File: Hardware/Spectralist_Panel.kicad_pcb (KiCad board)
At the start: 2 copper layers, 60.8 x 128.5 mm, 24 parts

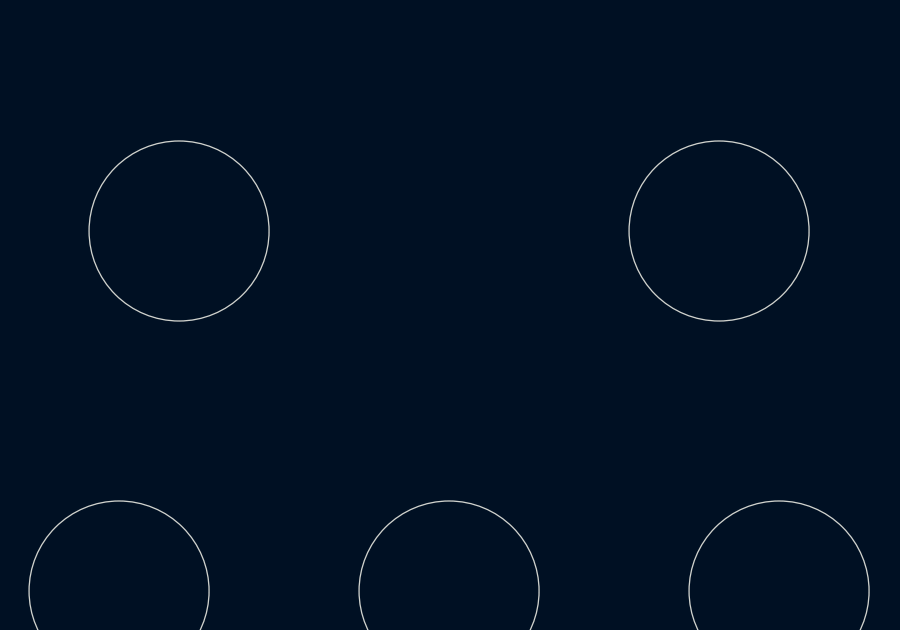
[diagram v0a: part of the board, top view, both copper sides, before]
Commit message: Schematic updates
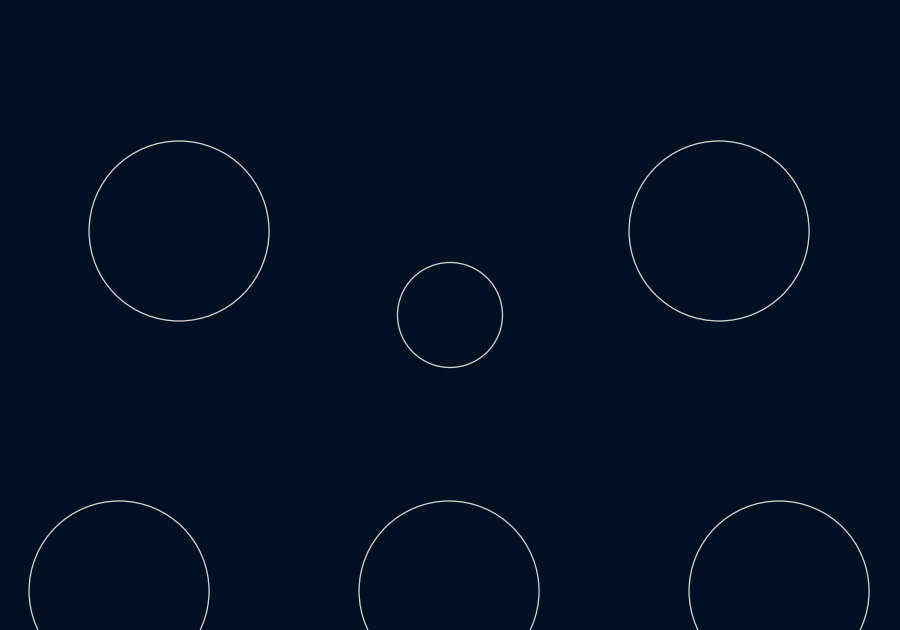
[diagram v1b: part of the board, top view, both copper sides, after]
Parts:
- added Ref**: Push_Button_Hole, Custom_Footprints:Small_Pushbutton_Hole_3.5mm, F.Cu at (130.0, 143.8)
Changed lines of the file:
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@@
+		)
+	)
+	(footprint "Custom_Footprints:Small_Pushbutton_Hole_3.5mm"
+		(layer "F.Cu")
+		(at 130.031383 143.8)
+		(descr "Button Hole 3.5mm")
+		(property "Reference" "Ref**"
+			(at 0 -5.4 0)
+			(layer "F.SilkS")
+			(hide yes)
+			(effects
+				(font
+					(size 1 1)
+					(thickness 0.15)
+				)
+			)
+		)
+		(property "Value" "Push_Button_Hole"
+			(at 0 5.1 0)
+			(layer "F.Fab")
+			(hide yes)
+			(effects
+				(font
+					(size 1 1)
+					(thickness 0.15)
+				)
+			)
+		)
+		(property "Footprint" "Custom_Footprints:Small_Pushbutton_Hole_3.5mm"
+			(at 0 0 0)
+			(unlocked yes)
+			(layer "F.Fab")
+			(hide yes)
+			(effects
+				(font
+					(size 1.27 1.27)
+					(thickness 0.15)
+				)
+			)
+		)
+		(property "Datasheet" ""
+			(at 0 0 0)
+			(unlocked yes)
+			(layer "F.Fab")
+			(hide yes)
+			(effects
+				(font
+					(size 1.27 1.27)
+					(thickness 0.15)
+				)
+			)
+		)
+		(property "Description" ""
+			(at 0 0 0)
+			(unlocked yes)
+			(layer "F.Fab")
+			(hide yes)
+			(effects
+				(font
+					(size 1.27 1.27)
+					(thickness 0.15)
+				)
+			)
+		)
+		(attr through_hole)
+		(fp_circle
+			(center 0 0)
+			(end 1.5 0)
+			(stroke
+				(width 0.15)
+				(type solid)
+			)
+			(fill none)
+			(layer "Cmts.User")
+		)
+		(fp_circle
+			(center 0 0)
+			(end 1.6 0)
+			(stroke
+				(width 0.05)
+				(type solid)
+			)
+			(fill none)
+			(layer "F.CrtYd")
+		)
+		(pad "" np_thru_hole circle
+			(at 0 0)
+			(size 3.5 3.5)
+			(drill 3.5)
+			(layers "*.Cu" "*.Mask")
+		)
+		(model "${KISYS3DMOD}/Button_Switch_THT.3dshapes/SW_PUSH_6mm_H13mm.wrl"
+			(offset
+				(xyz -3.15 2.25 -11.5)
+			)
+			(scale
+				(xyz 1 1 1)
+			)
+			(rotate
+				(xyz 0 0 0)
+			)
 		)
 	)
@@
 		(layer "F.Mask")
 	)
+	(gr_circle
+		(center 130.031383 137.4)
+		(end 131.931383 136.7)
+		(stroke
+			(width 0.1)
+			(type solid)
+		)
+		(fill solid)
+		(layer "F.Mask")
+	)
 	(gr_line
 		(start 108 91)
@@
 		)
 		(fill solid)
+		(layer "F.Mask")
+	)
+	(gr_line
+		(start 130.031383 137.4)
+		(end 130.031383 143.8)
+		(stroke
+			(width 0.6)
+			(type default)
+		)
 		(layer "F.Mask")
 	)
@@
 		(layer "F.Mask")
 	)
+	(gr_circle
+		(center 129.9 102.1)
+		(end 141.84 102.1)
+		(stroke
+			(width 2)
+			(type default)
+		)
+		(fill none)
+		(layer "F.Mask")
+	)
 	(gr_line
 		(start 105.8 108)
@@
 	)
 	(gr_circle
-		(center 198 96)
-		(end 198 113)
+		(center 193.1 100.598803)
+		(end 192.9 117.298803)
 		(stroke
 			(width 2)
@@
 		(stroke
 			(width 0.1)
+			(type solid)
+		)
+		(fill solid)
+		(layer "F.Mask")
+	)
+	(gr_circle
+		(center 130.031383 143.8)
+		(end 132.809558 143.8)
+		(stroke
+			(width 0.15)
 			(type solid)
 		)
@@
 		(net 0)
 		(net_name "")
+		(layers "F&B.Cu" "F.Mask")
+		(hatch edge 0.5)
+		(connect_pads
+			(clearance 0)
+		)
+		(min_thickness 0.25)
+		(filled_areas_thickness no)
+		(keepout
+			(tracks not_allowed)
+			(vias not_allowed)
+			(pads not_allowed)
+			(copperpour not_allowed)
+			(footprints allowed)
+		)
+		(fill
+			(thermal_gap 0.5)
+			(thermal_bridge_width 0.5)
+		)
+		(polygon
+			(pts
+				(xy 128.897317 136.260871) (xy 129.440323 135.896166) (xy 130.031382 135.794937) (xy 130.664606 135.8969)
+				(xy 131.162192 136.264128) (xy 131.530824 136.76208) (xy 131.631383 137.394937) (xy 131.531906 137.987115)
+				(xy 131.163582 138.527136) (xy 130.66491 138.852581) (xy 130.031383 138.994937) (xy 129.440316 138.852596)
+				(xy 128.9 138.52632) (xy 128.574409 137.986667) (xy 128.431383 137.394937) (xy 128.570888 136.760621)
+			)
+		)
+	)
+	(zone
+		(net 0)
+		(net_name "")
 		(layers "*.Mask")
 		(hatch edge 0.5)
@@
 			)
 		)
+	)
+	(zone
+		(net 0)
+		(net_name "")
+		(layers "*.Mask")
+		(hatch edge 0.5)
+		(connect_pads
+			(clearance 0)
+		)
+		(min_thickness 0.25)
+		(filled_areas_thickness no)
+		(fill yes
+			(thermal_gap 0.5)
+			(thermal_bridge_width 0.5)
+			(smoothing fillet)
+			(radius 10)
+		)
+		(polygon
+			(pts
+				(xy 128.570888 136.760621) (xy 128.897317 136.260871) (xy 129.440323 135.896166) (xy 130.031383 135.794937)
+				(xy 130.664606 135.8969) (xy 131.162192 136.264128) (xy 131.530824 136.76208) (xy 131.631383 137.394937)
+				(xy 131.531906 137.987115) (xy 131.163582 138.527136) (xy 130.66491 138.852581) (xy 130.031383 138.994937)
+				(xy 129.440316 138.852596) (xy 128.9 138.52632) (xy 128.574409 137.986667) (xy 128.431383 137.394937)
+			)
+		)

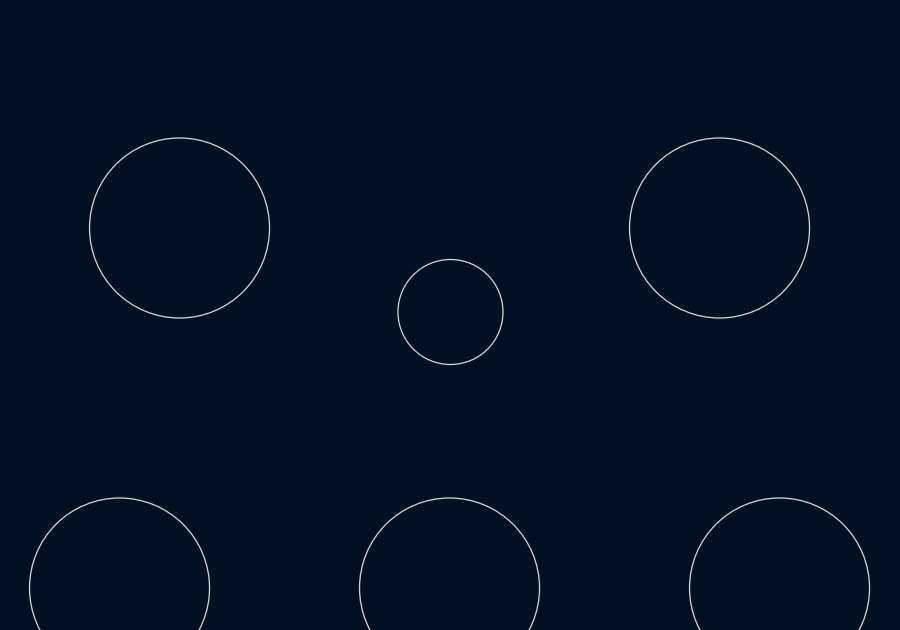
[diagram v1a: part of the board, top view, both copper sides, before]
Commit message: Schematic updates
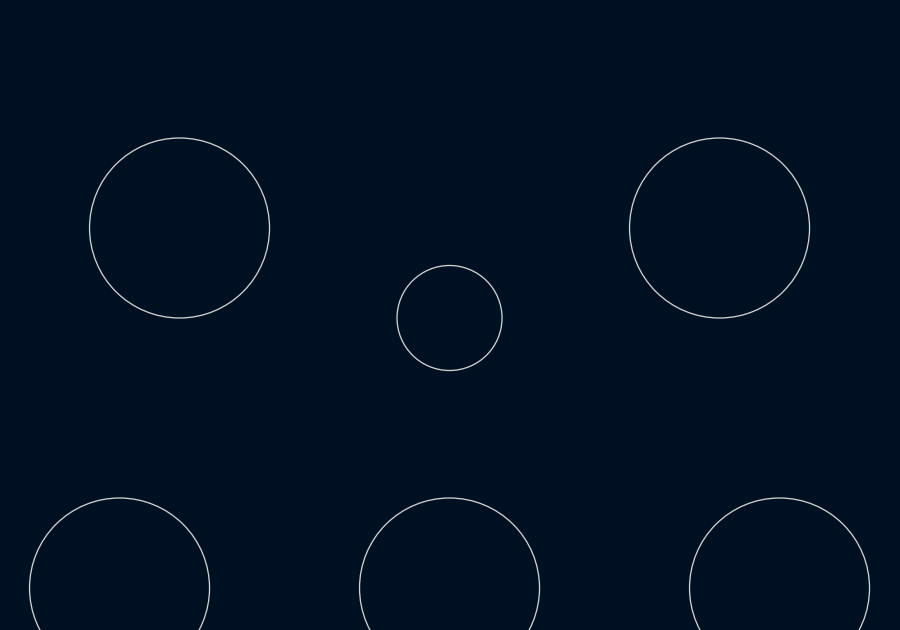
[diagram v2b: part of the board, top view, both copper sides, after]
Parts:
- moved Ref** 0.20 mm to (130.0, 144.0)
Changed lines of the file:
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@@
 	(footprint "Custom_Footprints:Small_Pushbutton_Hole_3.5mm"
 		(layer "F.Cu")
-		(at 130.031383 143.8)
+		(at 130 144)
 		(descr "Button Hole 3.5mm")
 		(property "Reference" "Ref**"
@@
 	)
 	(gr_circle
-		(center 130.031383 137.4)
-		(end 131.931383 136.7)
+		(center 130 137.4)
+		(end 131.9 136.7)
 		(stroke
 			(width 0.1)
@@
 	)
 	(gr_circle
-		(center 129.9 102.1)
-		(end 141.84 102.1)
+		(center 130 102)
+		(end 141.94 102)
 		(stroke
 			(width 2)
@@
 	)
 	(gr_circle
-		(center 193.1 100.598803)
-		(end 192.9 117.298803)
+		(center 204.8 100.098803)
+		(end 204.6 116.798803)
 		(stroke
 			(width 2)
@@
 	)
 	(gr_circle
-		(center 130.031383 143.8)
-		(end 132.809558 143.8)
+		(center 130 144)
+		(end 132.778175 144)
 		(stroke
 			(width 0.15)
@@
 	)
 	(gr_circle
-		(center 130 127.978175)
-		(end 130 123.978175)
-		(stroke
-			(width 0.15)
+		(center 130 128)
+		(end 130 124)
+		(stroke
+			(width 0.15)

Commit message: More PCB Layout
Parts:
- moved Ref** 2.00 mm to (130.0, 142.0)
- moved Ref** 1.41 mm to (140.0, 140.0)
- moved Ref** 1.41 mm to (120.0, 140.0)
- moved Ref** 1.00 mm to (130.0, 127.0)
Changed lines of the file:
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@@
 	(footprint "Custom_Footprints:Thonkiconn_Socket_MountingHole_6mm"
 		(layer "F.Cu")
-		(at 139 141 180)
+		(at 140 140 180)
 		(descr "Mounting Hole 6mm, no annular")
 		(tags "mounting hole 6mm no annular")
@@
 	(footprint "Custom_Footprints:Thonkiconn_Socket_MountingHole_6mm"
 		(layer "F.Cu")
-		(at 121 141 180)
+		(at 120 140 180)
 		(descr "Mounting Hole 6mm, no annular")
 		(tags "mounting hole 6mm no annular")
@@
 	(footprint "Custom_Footprints:Tall_Trimmer_Hole"
 		(layer "F.Cu")
-		(at 130 128)
+		(at 130 127)
 		(descr "Mounting Hole 6.5mm")
 		(tags "mounting hole 6.5mm")
@@
 	(footprint "Custom_Footprints:Small_Pushbutton_Hole_3.5mm"
 		(layer "F.Cu")
-		(at 130 144)
+		(at 130 142)
 		(descr "Button Hole 3.5mm")
 		(property "Reference" "Ref**"
@@
 	)
 	(gr_circle
-		(center 130 137.4)
-		(end 131.9 136.7)
+		(center 130 136)
+		(end 131.9 135.3)
 		(stroke
 			(width 0.1)
@@
 	)
 	(gr_line
-		(start 102.5 108.5)
-		(end 104 107)
+		(start 103.65 107.05)
+		(end 105.15 105.55)
 		(stroke
 			(width 1.2)
@@
 	)
 	(gr_line
-		(start 104 107)
-		(end 105.8 108)
+		(start 105.15 105.55)
+		(end 106.95 106.55)
 		(stroke
 			(width 1.2)
@@
 	)
 	(gr_line
-		(start 105.8 108)
-		(end 102.5 108.5)
+		(start 106.95 106.55)
+		(end 103.65 107.05)
 		(stroke
 			(width 1.2)
@@
 	)
 	(gr_arc
-		(start 130.031754 128.332425)
-		(mid 112.62064 123.029678)
-		(end 104.000001 107)
+		(start 130.4 142.2)
+		(mid 125.484153 141.374285)
+		(end 120.870299 139.487569)
+		(stroke
+			(width 1)
+			(type default)
+		)
+		(layer "F.Mask")
+	)
+	(gr_arc
+		(start 130.031754 127)
+		(mid 113.510184 122.044122)
+		(end 105.319064 106.864249)
 		(stroke
 			(width 1)
@@
 	)
 	(gr_circle
-		(center 130 144)
-		(end 132.778175 144)
+		(center 130 142)
+		(end 132.778175 142)
 		(stroke
 			(width 0.15)
@@
 	)
 	(gr_circle
-		(center 130 128)
-		(end 130 124)
+		(center 130 127)
+		(end 130 123)
 		(stroke
 			(width 0.15)
@@
 		(layer "Dwgs.User")
 	)
+	(gr_poly
+		(pts
+			(xy 110 101) (xy 114 101) (xy 114 92) (xy 114 82) (xy 146 82) (xy 146 101) (xy 150 101) (xy 150 115)
+			(xy 142 115) (xy 142 119) (xy 118 119) (xy 118 115) (xy 110 115)
+		)
+		(stroke
+			(width 0.05)
+			(type solid)
+		)
+		(fill none)
+		(layer "Dwgs.User")
+	)
+	(gr_rect
+		(start 127 97.55)
+		(end 133 106.45)
+		(stroke
+			(width 0.05)
+			(type default)
+		)
+		(fill none)
+		(layer "Dwgs.User")
+	)
 	(gr_line
 		(start 130 175.3)
@@
 	)
 	(gr_text "V/Oct"
-		(at 121 135.5 0)
+		(at 120 134.5 0)
 		(layer "F.Mask")
 		(effects
@@
 	)
 	(gr_text "Slope"
-		(at 139 135.5 0)
+		(at 140 134.5 0)
 		(layer "F.Mask")
 		(effects
@@
 		(polygon
 			(pts
-				(xy 128.897317 136.260871) (xy 129.440323 135.896166) (xy 130.031382 135.794937) (xy 130.664606 135.8969)
-				(xy 131.162192 136.264128) (xy 131.530824 136.76208) (xy 131.631383 137.394937) (xy 131.531906 137.987115)
-				(xy 131.163582 138.527136) (xy 130.66491 138.852581) (xy 130.031383 138.994937) (xy 129.440316 138.852596)
-				(xy 128.9 138.52632) (xy 128.574409 137.986667) (xy 128.431383 137.394937) (xy 128.570888 136.760621)
+				(xy 128.897317 134.860871) (xy 129.440323 134.496166) (xy 130.031382 134.394937) (xy 130.664606 134.4969)
+				(xy 131.162192 134.864128) (xy 131.530824 135.36208) (xy 131.631383 135.994937) (xy 131.531906 136.587115)
+				(xy 131.163582 137.127136) (xy 130.66491 137.452581) (xy 130.031383 137.594937) (xy 129.440316 137.452596)
+				(xy 128.9 137.12632) (xy 128.574409 136.586667) (xy 128.431383 135.994937) (xy 128.570888 135.360621)
 			)
 		)
@@
 		(polygon
 			(pts
-				(xy 128.570888 136.760621) (xy 128.897317 136.260871) (xy 129.440323 135.896166) (xy 130.031383 135.794937)
-				(xy 130.664606 135.8969) (xy 131.162192 136.264128) (xy 131.530824 136.76208) (xy 131.631383 137.394937)
-				(xy 131.531906 137.987115) (xy 131.163582 138.527136) (xy 130.66491 138.852581) (xy 130.031383 138.994937)
-				(xy 129.440316 138.852596) (xy 128.9 138.52632) (xy 128.574409 137.986667) (xy 128.431383 137.394937)
+				(xy 128.570888 135.360621) (xy 128.897317 134.860871) (xy 129.440323 134.496166) (xy 130.031383 134.394937)
+				(xy 130.664606 134.4969) (xy 131.162192 134.864128) (xy 131.530824 135.36208) (xy 131.631383 135.994937)
+				(xy 131.531906 136.587115) (xy 131.163582 137.127136) (xy 130.66491 137.452581) (xy 130.031383 137.594937)
+				(xy 129.440316 137.452596) (xy 128.9 137.12632) (xy 128.574409 136.586667) (xy 128.431383 135.994937)
 			)
 		)

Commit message: More PCB layout
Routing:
- added copper zone on F.Cu, net GND
- removed copper zone on F.Cu, net (none)
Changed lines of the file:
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@@
 			(drillshape 0)
 			(scaleselection 1)
-			(outputdirectory "Gerbers/Sinosaur_Panel/")
+			(outputdirectory "Gerbers/Spectralist_Panel/")
 		)
 	)
 	(net 0 "")
+	(net 1 "GND")
 	(footprint "Custom_Footprints:Alpha_9mm_pot_hole"
 		(layer "F.Cu")
@@
 		)
 	)
+	(gr_circle
+		(center 130 102)
+		(end 141.32 102)
+		(stroke
+			(width 0.1)
+			(type solid)
+		)
+		(fill solid)
+		(layer "F.Cu")
+		(net 1)
+	)
+	(gr_circle
+		(center 130 102)
+		(end 145.6 102)
+		(stroke
+			(width 6)
+			(type default)
+		)
+		(fill none)
+		(layer "F.Cu")
+		(net 1)
+	)
+	(gr_circle
+		(center 130 102)
+		(end 142 102)
+		(stroke
+			(width 2)
+			(type default)
+		)
+		(fill none)
+		(layer "B.Cu")
+	)
 	(gr_rect
 		(start 115.9 41.6)
@@
 		(layer "F.Mask")
 	)
+	(gr_arc
+		(start 123.841076 112.264874)
+		(mid 130.034299 90.029252)
+		(end 136.1 112.299999)
+		(stroke
+			(width 1.5)
+			(type default)
+		)
+		(layer "F.Mask")
+	)
 	(gr_line
 		(start 131 96)
@@
 		(layer "F.Mask")
 	)
-	(gr_circle
-		(center 130 102)
-		(end 141.94 102)
-		(stroke
-			(width 2)
-			(type default)
-		)
-		(fill none)
-		(layer "F.Mask")
-	)
 	(gr_line
 		(start 106.95 106.55)
@@
 		(layer "F.Mask")
 	)
-	(gr_circle
-		(center 204.8 100.098803)
-		(end 204.6 116.798803)
-		(stroke
-			(width 2)
-			(type default)
-		)
-		(fill none)
-		(layer "F.Mask")
-	)
 	(gr_line
 		(start 139.5 125.9)
@@
 	)
 	(gr_arc
-		(start 125 117.999999)
-		(mid 130 85.236946)
-		(end 135 117.999999)
-		(stroke
-			(width 2)
-			(type default)
-		)
-		(layer "F.Mask")
-	)
-	(gr_arc
 		(start 130.4 142.2)
 		(mid 125.484153 141.374285)
@@
 	)
 	(zone
-		(net 0)
-		(net_name "")
-		(locked yes)
-		(layers "F&B.Cu")
+		(net 1)
+		(net_name "GND")
+		(layer "F.Cu")
 		(hatch edge 0.508)
-		(connect_pads
+		(priority 1)
+		(connect_pads yes
 			(clearance 0)
 		)
-		(min_thickness 0.254)
+		(min_thickness 0.025)
 		(filled_areas_thickness no)
 		(fill yes
-			(thermal_gap 0.508)
-			(thermal_bridge_width 0.508)
+			(thermal_gap 0)
+			(thermal_bridge_width 0.025)
+			(island_removal_mode 1)
+			(island_area_min 10)
 		)
 		(polygon
 			(pts
-				(xy 162.6 172.8) (xy 96.6 172.8) (xy 96.6 38.8) (xy 162.6 38.8)
+				(xy 97.9 40.3) (xy 161.9 40.7) (xy 161.8 173) (xy 142.8 173) (xy 142.8 89) (xy 116.8 89) (xy 116.8 114)
+				(xy 122.7 114) (xy 123.7 113) (xy 124.105385 112.906923) (xy 124.4 112.6) (xy 124.475385 112.2)
+				(xy 124.1 111) (xy 135.8 111) (xy 135.5 112) (xy 135.5 112.2) (xy 135.5 112.5) (xy 135.7 112.8)
+				(xy 136 112.9) (xy 136.2 112.9) (xy 137 113.1) (xy 137.4 113.8) (xy 142.8 114) (xy 142.8 173) (xy 97.8 173)
+				(xy 98 40.3)
 			)
 		)
@@
 			)
 		)
+	)
+	(zone
+		(net 0)
+		(net_name "")
+		(layer "B.Cu")
+		(hatch edge 0.508)
+		(priority 2)
+		(connect_pads
+			(clearance 0)
+		)
+		(min_thickness 0.254)
+		(filled_areas_thickness no)
+		(fill yes
+			(thermal_gap 0.508)
+			(thermal_bridge_width 0.508)
+			(island_removal_mode 1)
+			(island_area_min 10)
+		)
+		(polygon
+			(pts
+				(xy 162 171) (xy 98 171) (xy 98 39) (xy 162 39)
+			)
+		)
